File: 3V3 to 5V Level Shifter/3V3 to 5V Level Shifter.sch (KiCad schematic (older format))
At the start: 17 parts, among them J1001 Conn_01x02_Male, J1002 Conn_01x04_Male, J1003 Conn_01x04_Male, J1004 Conn_01x04_Male, J1005 Conn_01x04_Male, U1001 74LVC125, U1002 74LVC125

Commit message: Finishing design
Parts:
- added J1006: Conn_01x02_Male, Connector_PinHeader_2.54mm:PinHeader_1x02_P2.54mm_Vertical, symbol Connector:Conn_01x02_Male
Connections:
- net +5V: now also J1006.1 (Pin_1)
- net GND: now also J1006.2 (Pin_2)
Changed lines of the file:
@@
 Wire Wire Line
 	6600 3500 6700 3500
+$Comp
+L Connector:Conn_01x02_Male J1006
+U 1 1 619EA8F0
+P 2900 1250
+F 0 "J1006" H 3008 1431 50  0000 C CNN
+F 1 "Conn_01x02_Male" H 3008 1340 50  0000 C CNN
+F 2 "Connector_PinHeader_2.54mm:PinHeader_1x02_P2.54mm_Vertical" H 2900 1250 50  0001 C CNN
+F 3 "~" H 2900 1250 50  0001 C CNN
+	1    2900 1250
+	-1   0    0    -1
+$EndComp
+Wire Wire Line
+	2300 1250 2700 1250
+Connection ~ 2300 1250
+Wire Wire Line
+	2300 1350 2700 1350
+Connection ~ 2300 1350
 $EndSCHEMATC

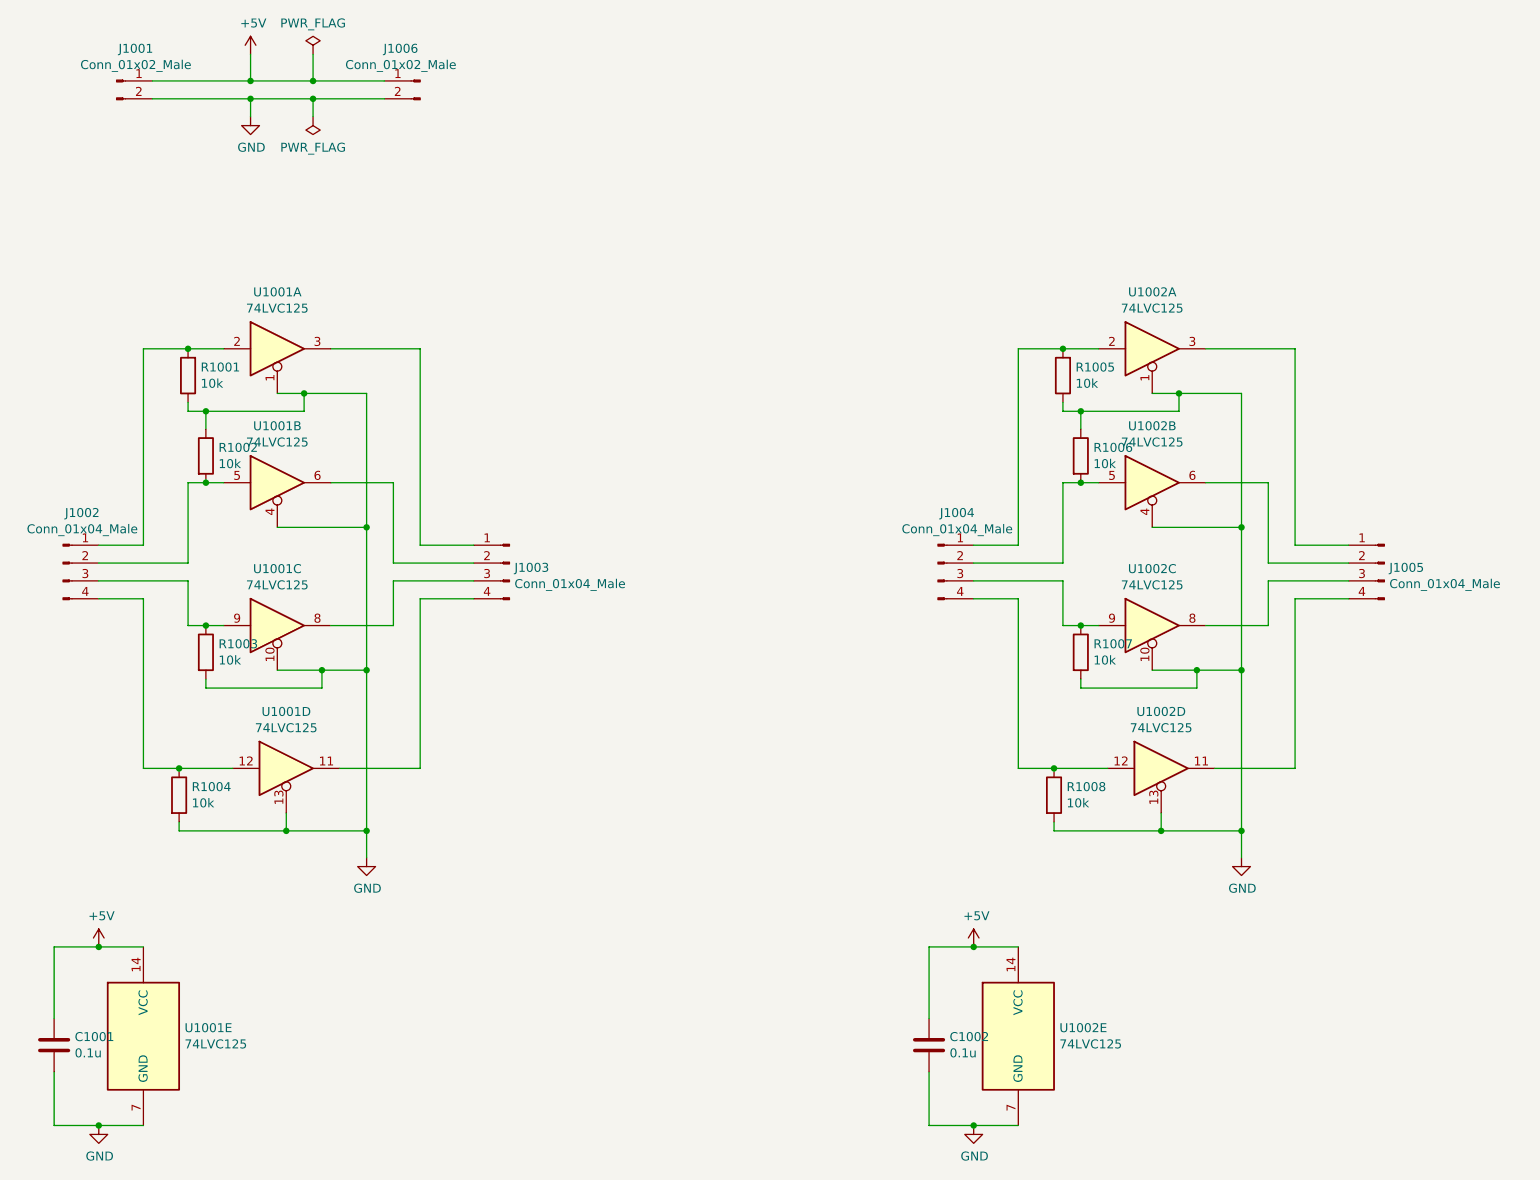
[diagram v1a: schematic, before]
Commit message: Correct IC name
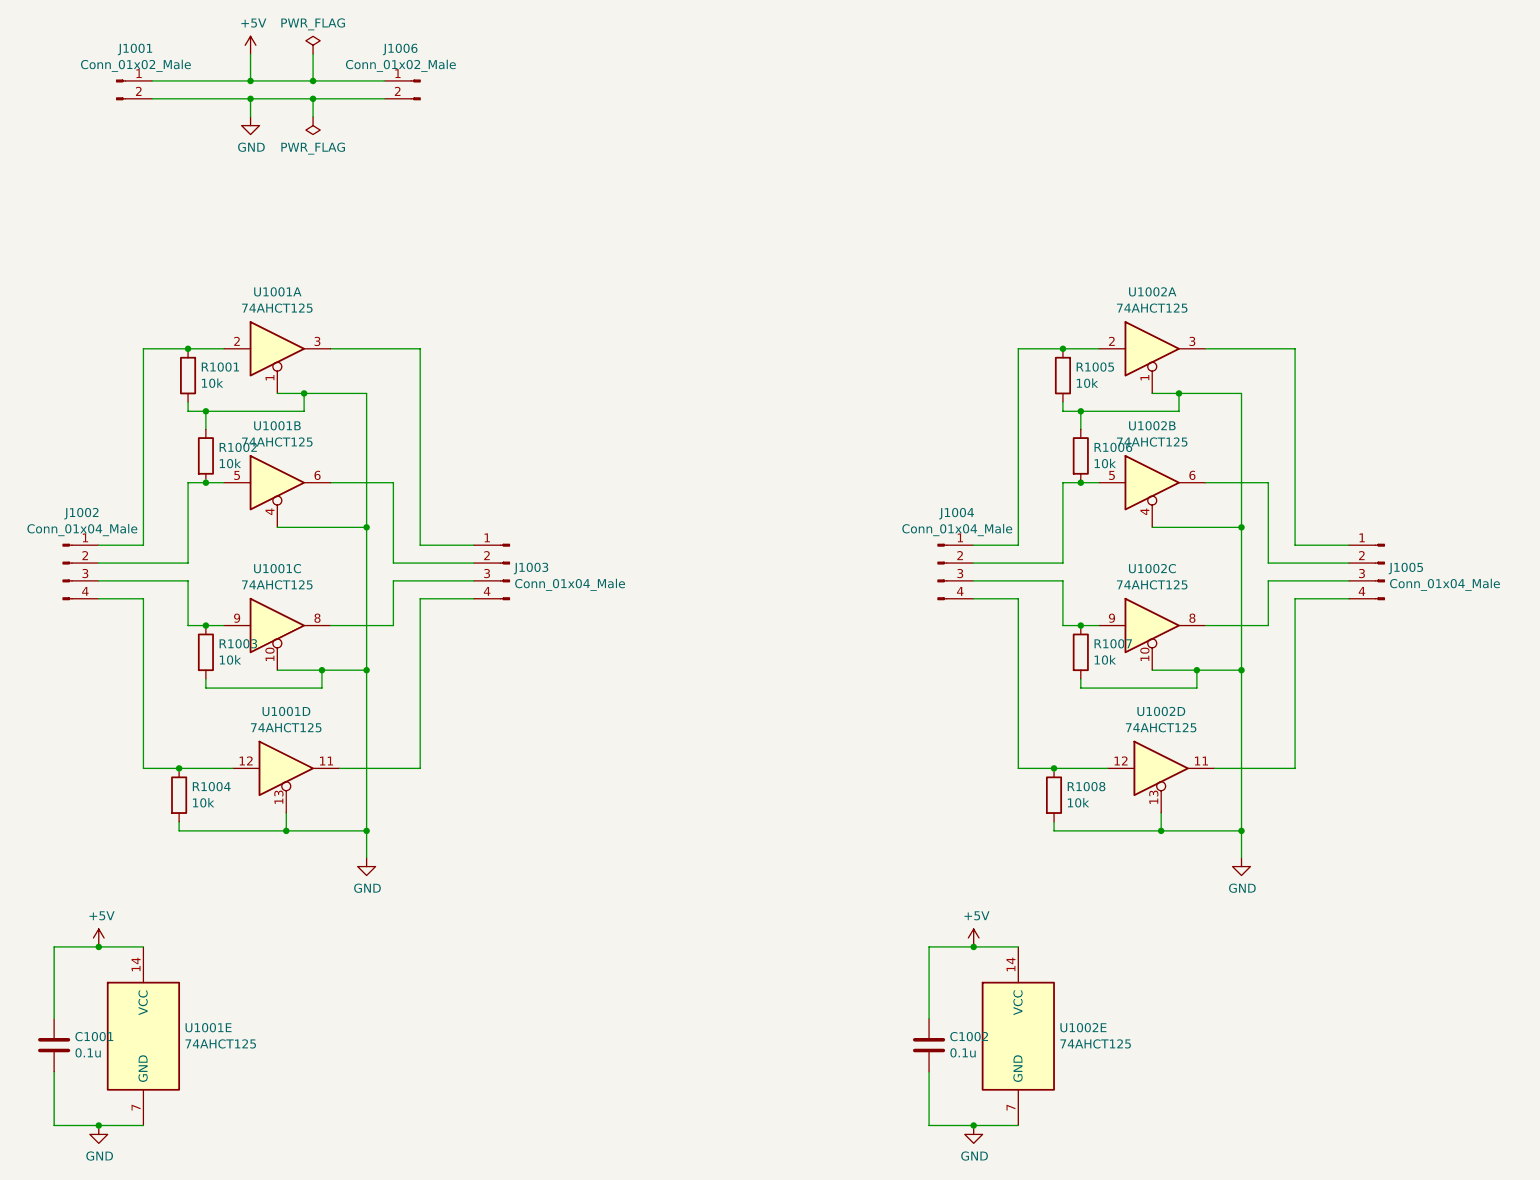
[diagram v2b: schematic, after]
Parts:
- U1001, U1002: value 74LVC125 -> 74AHCT125
- U1001, U1002: value 74LVC125 -> 74AHCT125; footprint (none) -> Package_DIP:DIP-14_W7.62mm_Socket
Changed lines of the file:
@@
 P 2100 2750
 F 0 "U1001" H 2100 3067 50  0000 C CNN
-F 1 "74LVC125" H 2100 2976 50  0000 C CNN
+F 1 "74AHCT125" H 2100 2976 50  0000 C CNN
 F 2 "Package_DIP:DIP-14_W7.62mm_Socket" H 2100 2750 50  0001 C CNN
 F 3 "http://www.ti.com/lit/gpn/sn74LVC125" H 2100 2750 50  0001 C CNN
@@
 P 2100 3500
 F 0 "U1001" H 2100 3817 50  0000 C CNN
-F 1 "74LVC125" H 2100 3726 50  0000 C CNN
-F 2 "" H 2100 3500 50  0001 C CNN
+F 1 "74AHCT125" H 2100 3726 50  0000 C CNN
+F 2 "Package_DIP:DIP-14_W7.62mm_Socket" H 2100 3500 50  0001 C CNN
 F 3 "http://www.ti.com/lit/gpn/sn74LVC125" H 2100 3500 50  0001 C CNN
 	2    2100 3500
@@
 P 2100 4300
 F 0 "U1001" H 2100 4617 50  0000 C CNN
-F 1 "74LVC125" H 2100 4526 50  0000 C CNN
-F 2 "" H 2100 4300 50  0001 C CNN
+F 1 "74AHCT125" H 2100 4526 50  0000 C CNN
+F 2 "Package_DIP:DIP-14_W7.62mm_Socket" H 2100 4300 50  0001 C CNN
 F 3 "http://www.ti.com/lit/gpn/sn74LVC125" H 2100 4300 50  0001 C CNN
 	3    2100 4300
@@
 P 2150 5100
 F 0 "U1001" H 2150 5417 50  0000 C CNN
-F 1 "74LVC125" H 2150 5326 50  0000 C CNN
-F 2 "" H 2150 5100 50  0001 C CNN
+F 1 "74AHCT125" H 2150 5326 50  0000 C CNN
+F 2 "Package_DIP:DIP-14_W7.62mm_Socket" H 2150 5100 50  0001 C CNN
 F 3 "http://www.ti.com/lit/gpn/sn74LVC125" H 2150 5100 50  0001 C CNN
 	4    2150 5100
@@
 P 1350 6600
 F 0 "U1001" H 1580 6646 50  0000 L CNN
-F 1 "74LVC125" H 1580 6555 50  0000 L CNN
-F 2 "" H 1350 6600 50  0001 C CNN
+F 1 "74AHCT125" H 1580 6555 50  0000 L CNN
+F 2 "Package_DIP:DIP-14_W7.62mm_Socket" H 1350 6600 50  0001 C CNN
 F 3 "http://www.ti.com/lit/gpn/sn74LVC125" H 1350 6600 50  0001 C CNN
 	5    1350 6600
@@
 P 7000 2750
 F 0 "U1002" H 7000 3067 50  0000 C CNN
-F 1 "74LVC125" H 7000 2976 50  0000 C CNN
+F 1 "74AHCT125" H 7000 2976 50  0000 C CNN
 F 2 "Package_DIP:DIP-14_W7.62mm_Socket" H 7000 2750 50  0001 C CNN
 F 3 "http://www.ti.com/lit/gpn/sn74LVC125" H 7000 2750 50  0001 C CNN
@@
 P 7000 3500
 F 0 "U1002" H 7000 3817 50  0000 C CNN
-F 1 "74LVC125" H 7000 3726 50  0000 C CNN
-F 2 "" H 7000 3500 50  0001 C CNN
+F 1 "74AHCT125" H 7000 3726 50  0000 C CNN
+F 2 "Package_DIP:DIP-14_W7.62mm_Socket" H 7000 3500 50  0001 C CNN
 F 3 "http://www.ti.com/lit/gpn/sn74LVC125" H 7000 3500 50  0001 C CNN
 	2    7000 3500
@@
 P 7000 4300
 F 0 "U1002" H 7000 4617 50  0000 C CNN
-F 1 "74LVC125" H 7000 4526 50  0000 C CNN
-F 2 "" H 7000 4300 50  0001 C CNN
+F 1 "74AHCT125" H 7000 4526 50  0000 C CNN
+F 2 "Package_DIP:DIP-14_W7.62mm_Socket" H 7000 4300 50  0001 C CNN
 F 3 "http://www.ti.com/lit/gpn/sn74LVC125" H 7000 4300 50  0001 C CNN
 	3    7000 4300
@@
 P 7050 5100
 F 0 "U1002" H 7050 5417 50  0000 C CNN
-F 1 "74LVC125" H 7050 5326 50  0000 C CNN
-F 2 "" H 7050 5100 50  0001 C CNN
+F 1 "74AHCT125" H 7050 5326 50  0000 C CNN
+F 2 "Package_DIP:DIP-14_W7.62mm_Socket" H 7050 5100 50  0001 C CNN
 F 3 "http://www.ti.com/lit/gpn/sn74LVC125" H 7050 5100 50  0001 C CNN
 	4    7050 5100
@@
 P 6250 6600
 F 0 "U1002" H 6480 6646 50  0000 L CNN
-F 1 "74LVC125" H 6480 6555 50  0000 L CNN
-F 2 "" H 6250 6600 50  0001 C CNN
+F 1 "74AHCT125" H 6480 6555 50  0000 L CNN
+F 2 "Package_DIP:DIP-14_W7.62mm_Socket" H 6250 6600 50  0001 C CNN
 F 3 "http://www.ti.com/lit/gpn/sn74LVC125" H 6250 6600 50  0001 C CNN
 	5    6250 6600
